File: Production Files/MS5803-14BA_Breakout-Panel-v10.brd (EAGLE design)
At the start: 117.3 x 104.6 mm, 428 parts, among them U1 MS5803-14BA, U10 MS5803-14BA, U11 MS5803-14BA, U12 MS5803-14BA, U13 MS5803-14BA, U14 MS5803-14BA, U15 MS5803-14BA, U16 MS5803-14BA, U17 MS5803-14BA, U18 MS5803-14BA, U19 MS5803-14BA, U2 MS5803-14BA, U20 MS5803-14BA, U21 MS5803-14BA, U22 MS5803-14BA, U23 MS5803-14BA, U24 MS5803-14BA, U25 MS5803-14BA, U3 MS5803-14BA, U4 MS5803-14BA, U5 MS5803-14BA, U6 MS5803-14BA, U7 MS5803-14BA, U8 MS5803-14BA, U9 MS5803-14BA

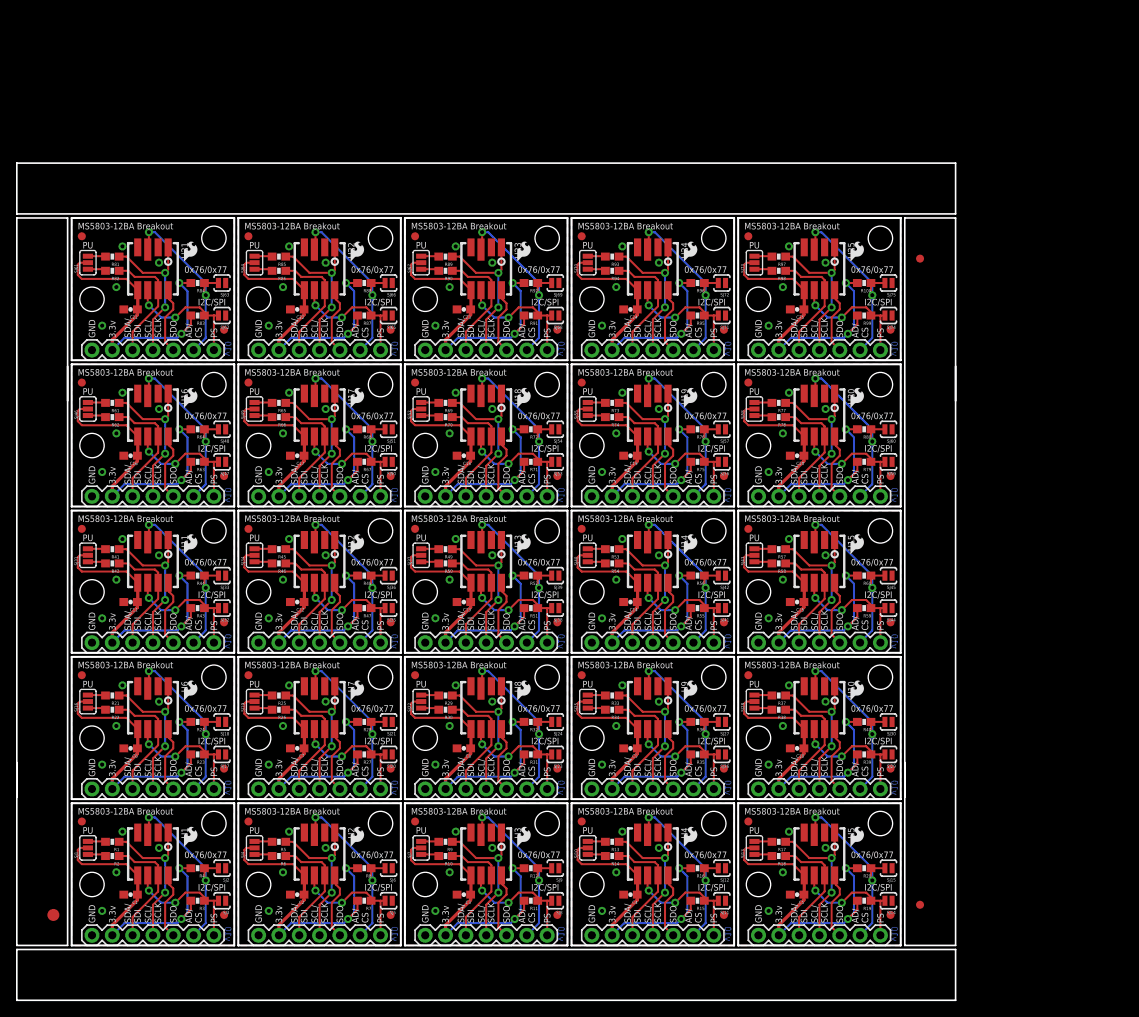
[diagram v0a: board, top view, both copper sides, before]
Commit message: re-created panel v10
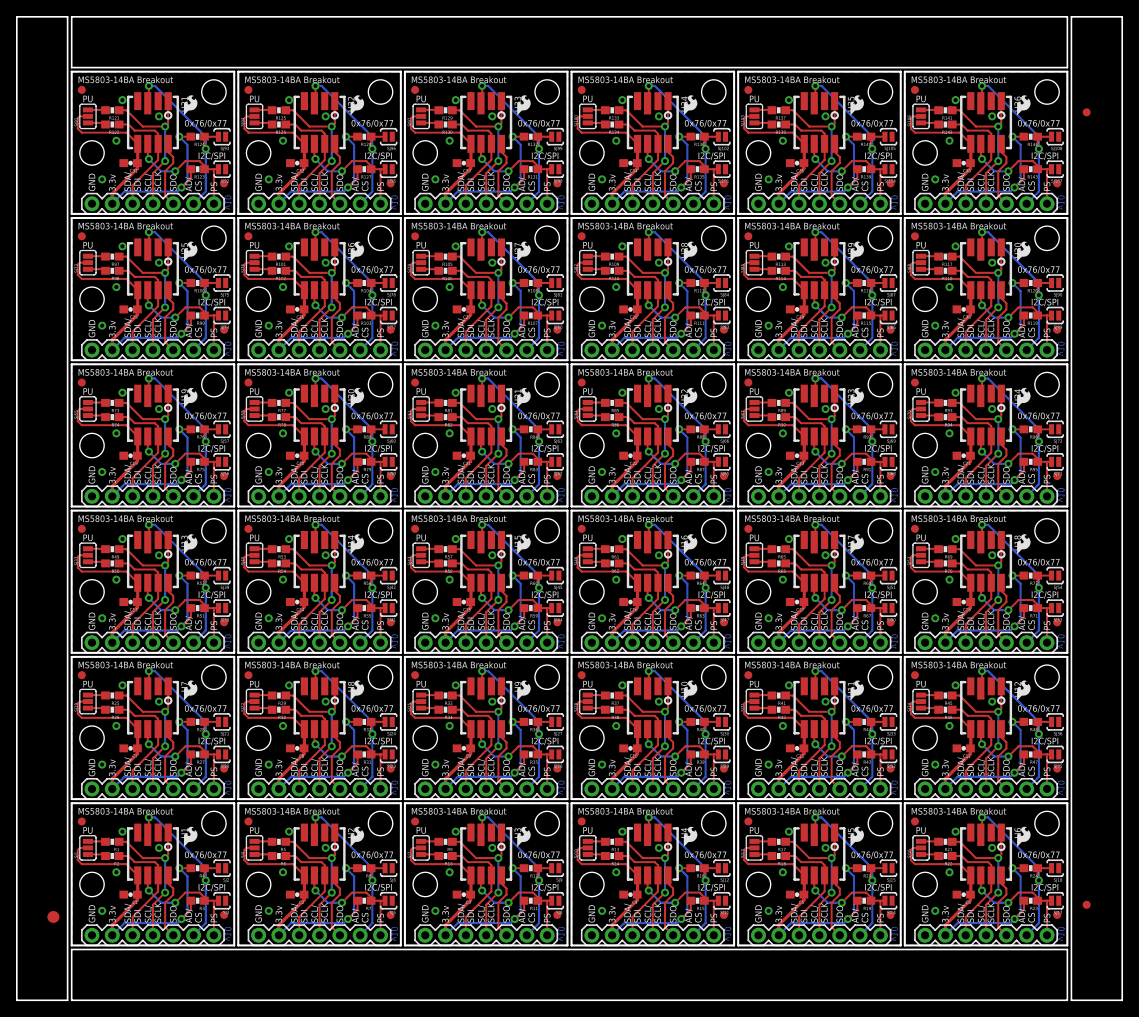
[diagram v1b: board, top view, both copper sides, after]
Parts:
- removed E$5: (no value), SparkFun-Aesthetics:FIDUCIAL-1X2
- added C26, C27, C28, C29, C30, C31, C32, C33, C34, C35, C36: 0.1uF, SparkFun-Capacitors:0603-CAP
- added E$6: (no value), SparkFun-Aesthetics:FIDUCIAL-1X2
- added FID51, FID52, FID53, FID54, FID55, FID56, FID57, FID58, FID59, FID60, FID61, FID62, FID63, FID64, FID65, FID66, FID67, FID68, FID69, FID70, FID71, FID72: FIDUCIAL1X2, SparkFun-Aesthetics:FIDUCIAL-1X2
- added JP26, JP27, JP28, JP29, JP30, JP31, JP32, JP33, JP34, JP35, JP36: (no value), SparkFun-Connectors:1X07
- added LOGO100, LOGO103, LOGO106, LOGO76, LOGO79, LOGO82, LOGO85, LOGO88, LOGO91, LOGO94, LOGO97: SFE_LOGO_FLAME.1_INCH, SparkFun-Aesthetics:SFE_LOGO_FLAME_.1
- added LOGO101, LOGO104, LOGO107, LOGO77, LOGO80, LOGO83, LOGO86, LOGO89, LOGO92, LOGO95, LOGO98: SFE_LOGO_NAME_FLAME.1_INCH, SparkFun-Aesthetics:SFE_LOGO_NAME_FLAME_.1
- added LOGO102, LOGO105, LOGO108, LOGO78, LOGO81, LOGO84, LOGO87, LOGO90, LOGO93, LOGO96, LOGO99: OSHW-LOGOS, SparkFun-Aesthetics:OSHW-LOGO-S
- added R101, R102, R105, R106, R109, R110, R113, R114, R117, R118, R121, R122, R125, R126, R129, R130, R133, R134, R137, R138, R141, R142: 2.2k, SparkFun-Resistors:0603-RES
- added R103, R104, R107, R108, R111, R112, R115, R116, R119, R120, R123, R124, R127, R128, R131, R132, R135, R136, R139, R140, R143, R144: 10K, SparkFun-Resistors:0603-RES
- added SJ100, SJ103, SJ106, SJ76, SJ79, SJ82, SJ85, SJ88, SJ91, SJ94, SJ97: (no value), SparkFun-Passives:PAD-JUMPER-3-NC_BY_PASTE_YES_SILK_FULL_BOX
- added SJ101, SJ102, SJ104, SJ105, SJ107, SJ108, SJ77, SJ78, SJ80, SJ81, SJ83, SJ84, SJ86, SJ87, SJ89, SJ90, SJ92, SJ93, SJ95, SJ96, SJ98, SJ99: SOLDERJUMPERNO, SparkFun-Passives:SJ_2S-NO
- added STANDOFF51, STANDOFF52, STANDOFF53, STANDOFF54, STANDOFF55, STANDOFF56, STANDOFF57, STANDOFF58, STANDOFF59, STANDOFF60, STANDOFF61, STANDOFF62, STANDOFF63, STANDOFF64, STANDOFF65, STANDOFF66, STANDOFF67, STANDOFF68, STANDOFF69, STANDOFF70, STANDOFF71, STANDOFF72: STAND-OFFTIGHT, SparkFun-Electromechanical:STAND-OFF-TIGHT
- added U26, U27, U28, U29, U30, U31, U32, U33, U34, U35, U36: MS5803-14BA, MS5803:MS5803
- moved SJ17 105.7 mm to (129.8, 12.4)
- moved SJ18 105.7 mm to (129.8, 16.5)
- moved C6 105.7 mm to (118.4, 13.2)
- moved FID11 105.7 mm to (130.0, 10.7)
- moved FID12 105.7 mm to (112.3, 22.4)
- moved JP6 105.7 mm to (113.5, 8.13)
- moved LOGO16 105.7 mm to (124.7, 18.8)
- moved LOGO17 105.7 mm to (127.5, 13.2)
- moved LOGO18 105.7 mm to (121.2, 20.8)
- moved R21 105.7 mm to (116.1, 19.8)
- moved R22 105.7 mm to (116.1, 18.0)
- moved SJ16 105.7 mm to (113.0, 19.1)
- moved STANDOFF11 105.7 mm to (113.5, 14.5)
- moved U6 105.7 mm to (121.2, 18.3)
- moved R23 105.7 mm to (126.7, 12.4)
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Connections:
- new net 3.3V25: C26.1, JP26.2, R103.2, R104.2, SJ76.2, U26.5
- new net 3.3V26: C27.1, JP27.2, R107.2, R108.2, SJ79.2, U27.5
- new net 3.3V27: C28.1, JP28.2, R111.2, R112.2, SJ82.2, U28.5
- new net 3.3V28: C29.1, JP29.2, R115.2, R116.2, SJ85.2, U29.5
- new net 3.3V29: C30.1, JP30.2, R119.2, R120.2, SJ88.2, U30.5
- new net 3.3V30: C31.1, JP31.2, R123.2, R124.2, SJ91.2, U31.5
- new net 3.3V31: C32.1, JP32.2, R127.2, R128.2, SJ94.2, U32.5
- new net 3.3V32: C33.1, JP33.2, R131.2, R132.2, SJ97.2, U33.5
- new net 3.3V33: C34.1, JP34.2, R135.2, R136.2, SJ100.2, U34.5
- new net 3.3V34: C35.1, JP35.2, R139.2, R140.2, SJ103.2, U35.5
- new net 3.3V35: C36.1, JP36.2, R143.2, R144.2, SJ106.2, U36.5
- new net AD/CS25: JP26.6, R104.1, SJ78.2, U26.3
- new net AD/CS26: JP27.6, R108.1, SJ81.2, U27.3
- new net AD/CS27: JP28.6, R112.1, SJ84.2, U28.3
- new net AD/CS28: JP29.6, R116.1, SJ87.2, U29.3
- new net AD/CS29: JP30.6, R120.1, SJ90.2, U30.3
- new net AD/CS30: JP31.6, R124.1, SJ93.2, U31.3
- new net AD/CS31: JP32.6, R128.1, SJ96.2, U32.3
- new net AD/CS32: JP33.6, R132.1, SJ99.2, U33.3
- new net AD/CS33: JP34.6, R136.1, SJ102.2, U34.3
- new net AD/CS34: JP35.6, R140.1, SJ105.2, U35.3
- new net AD/CS35: JP36.6, R144.1, SJ108.2, U36.3
- new net GND25: C26.2, JP26.1, SJ77.1, SJ78.1, U26.2
- new net GND26: C27.2, JP27.1, SJ80.1, SJ81.1, U27.2
- new net GND27: C28.2, JP28.1, SJ83.1, SJ84.1, U28.2
- new net GND28: C29.2, JP29.1, SJ86.1, SJ87.1, U29.2
- new net GND29: C30.2, JP30.1, SJ89.1, SJ90.1, U30.2
- new net GND30: C31.2, JP31.1, SJ92.1, SJ93.1, U31.2
- new net GND31: C32.2, JP32.1, SJ95.1, SJ96.1, U32.2
- new net GND32: C33.2, JP33.1, SJ98.1, SJ99.1, U33.2
- new net GND33: C34.2, JP34.1, SJ101.1, SJ102.1, U34.2
- new net GND34: C35.2, JP35.1, SJ104.1, SJ105.1, U35.2
- new net GND35: C36.2, JP36.1, SJ107.1, SJ108.1, U36.2
- new net N$51: R101.2, SJ76.3
- new net N$52: R102.2, SJ76.1
- new net N$53: R105.2, SJ79.3
- new net N$54: R106.2, SJ79.1
- new net N$55: R109.2, SJ82.3
- new net N$56: R110.2, SJ82.1
- new net N$57: R113.2, SJ85.3
- new net N$58: R114.2, SJ85.1
- new net N$59: R117.2, SJ88.3
- new net N$60: R118.2, SJ88.1
- new net N$61: R121.2, SJ91.3
- new net N$62: R122.2, SJ91.1
- new net N$63: R125.2, SJ94.3
- new net N$64: R126.2, SJ94.1
- new net N$65: R129.2, SJ97.3
- new net N$66: R130.2, SJ97.1
- new net N$67: R133.2, SJ100.3
- new net N$68: R134.2, SJ100.1
- new net N$69: R137.2, SJ103.3
- new net N$70: R138.2, SJ103.1
- new net N$71: R141.2, SJ106.3
- new net N$72: R142.2, SJ106.1
- new net PS25: JP26.7, R103.1, SJ77.2, U26.6
- new net PS26: JP27.7, R107.1, SJ80.2, U27.6
- new net PS27: JP28.7, R111.1, SJ83.2, U28.6
- new net PS28: JP29.7, R115.1, SJ86.2, U29.6
- new net PS29: JP30.7, R119.1, SJ89.2, U30.6
- new net PS30: JP31.7, R123.1, SJ92.2, U31.6
- new net PS31: JP32.7, R127.1, SJ95.2, U32.6
- new net PS32: JP33.7, R131.1, SJ98.2, U33.6
- new net PS33: JP34.7, R135.1, SJ101.2, U34.6
- new net PS34: JP35.7, R139.1, SJ104.2, U35.6
- new net PS35: JP36.7, R143.1, SJ107.2, U36.6
- new net SCL/SCLK25: JP26.4, R101.1, U26.1
- new net SCL/SCLK26: JP27.4, R105.1, U27.1
- new net SCL/SCLK27: JP28.4, R109.1, U28.1
- new net SCL/SCLK28: JP29.4, R113.1, U29.1
- new net SCL/SCLK29: JP30.4, R117.1, U30.1
- new net SCL/SCLK30: JP31.4, R121.1, U31.1
- new net SCL/SCLK31: JP32.4, R125.1, U32.1
- new net SCL/SCLK32: JP33.4, R129.1, U33.1
- new net SCL/SCLK33: JP34.4, R133.1, U34.1
- new net SCL/SCLK34: JP35.4, R137.1, U35.1
- new net SCL/SCLK35: JP36.4, R141.1, U36.1
- new net SDA/SDI25: JP26.3, R102.1, U26.7
- new net SDA/SDI26: JP27.3, R106.1, U27.7
- new net SDA/SDI27: JP28.3, R110.1, U28.7
- new net SDA/SDI28: JP29.3, R114.1, U29.7
- new net SDA/SDI29: JP30.3, R118.1, U30.7
- new net SDA/SDI30: JP31.3, R122.1, U31.7
- new net SDA/SDI31: JP32.3, R126.1, U32.7
- new net SDA/SDI32: JP33.3, R130.1, U33.7
- new net SDA/SDI33: JP34.3, R134.1, U34.7
- new net SDA/SDI34: JP35.3, R138.1, U35.7
- new net SDA/SDI35: JP36.3, R142.1, U36.7
- new net SDO25: JP26.5, U26.8
- new net SDO26: JP27.5, U27.8
- new net SDO27: JP28.5, U28.8
- new net SDO28: JP29.5, U29.8
- new net SDO29: JP30.5, U30.8
- new net SDO30: JP31.5, U31.8
- new net SDO31: JP32.5, U32.8
- new net SDO32: JP33.5, U33.8
- new net SDO33: JP34.5, U34.8
- new net SDO34: JP35.5, U35.8
- new net SDO35: JP36.5, U36.8
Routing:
- net 3.3V31: track 0.00 -> 40.6 mm, vias 0 -> 2
- net 3.3V30: track 0.00 -> 40.6 mm, vias 0 -> 2
- net 3.3V25: track 0.00 -> 40.6 mm, vias 0 -> 2
- net 3.3V35: track 0.00 -> 40.6 mm, vias 0 -> 2
- net 3.3V34: track 0.00 -> 40.6 mm, vias 0 -> 2
- net 3.3V32: track 0.00 -> 40.6 mm, vias 0 -> 2
- net 3.3V26: track 0.00 -> 40.6 mm, vias 0 -> 2
- net 3.3V33: track 0.00 -> 40.6 mm, vias 0 -> 2
- net 3.3V29: track 0.00 -> 40.6 mm, vias 0 -> 2
- net 3.3V28: track 0.00 -> 40.6 mm, vias 0 -> 2
- net 3.3V27: track 0.00 -> 40.6 mm, vias 0 -> 2
- net AD/CS32: track 0.00 -> 24.3 mm, vias 0 -> 2
- net AD/CS26: track 0.00 -> 24.3 mm, vias 0 -> 2
- net AD/CS31: track 0.00 -> 24.3 mm, vias 0 -> 2
- net AD/CS25: track 0.00 -> 24.3 mm, vias 0 -> 2
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- added copper zone on layer 1, net GND25
- added copper zone on layer 16, net GND25
- added copper zone on layer 1, net GND26
- added copper zone on layer 16, net GND26
- added copper zone on layer 1, net GND27
- added copper zone on layer 16, net GND27
- added copper zone on layer 1, net GND28
- added copper zone on layer 16, net GND28
- added copper zone on layer 1, net GND29
- added copper zone on layer 16, net GND29
- added copper zone on layer 1, net GND30
- added copper zone on layer 16, net GND30
- added copper zone on layer 1, net GND31
- added copper zone on layer 16, net GND31
- added copper zone on layer 1, net GND32
- added copper zone on layer 16, net GND32
- added copper zone on layer 1, net GND33
- added copper zone on layer 16, net GND33
- added copper zone on layer 1, net GND34
- added copper zone on layer 16, net GND34
- added copper zone on layer 1, net GND35
- added copper zone on layer 16, net GND35
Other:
- board size 117.3 x 104.6 mm -> 138.2 x 122.9 mm
- board text added: "MS5803-14BA Breakout"
- board text removed: "MS5803-12BA Breakout"
